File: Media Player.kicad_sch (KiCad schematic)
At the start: 33 parts, among them J1 PH2.0, J2 MEM2075-00-140-01-A, J3 USB_C_Receptacle_USB2.0_14P, SW1 SW_Push, SW2 SW_Push, SW3 SW_Push, SW4 SW_Push, SW5 SW_Push, SW6 SW_Push, U1 ESP32-S3-WROOM-1

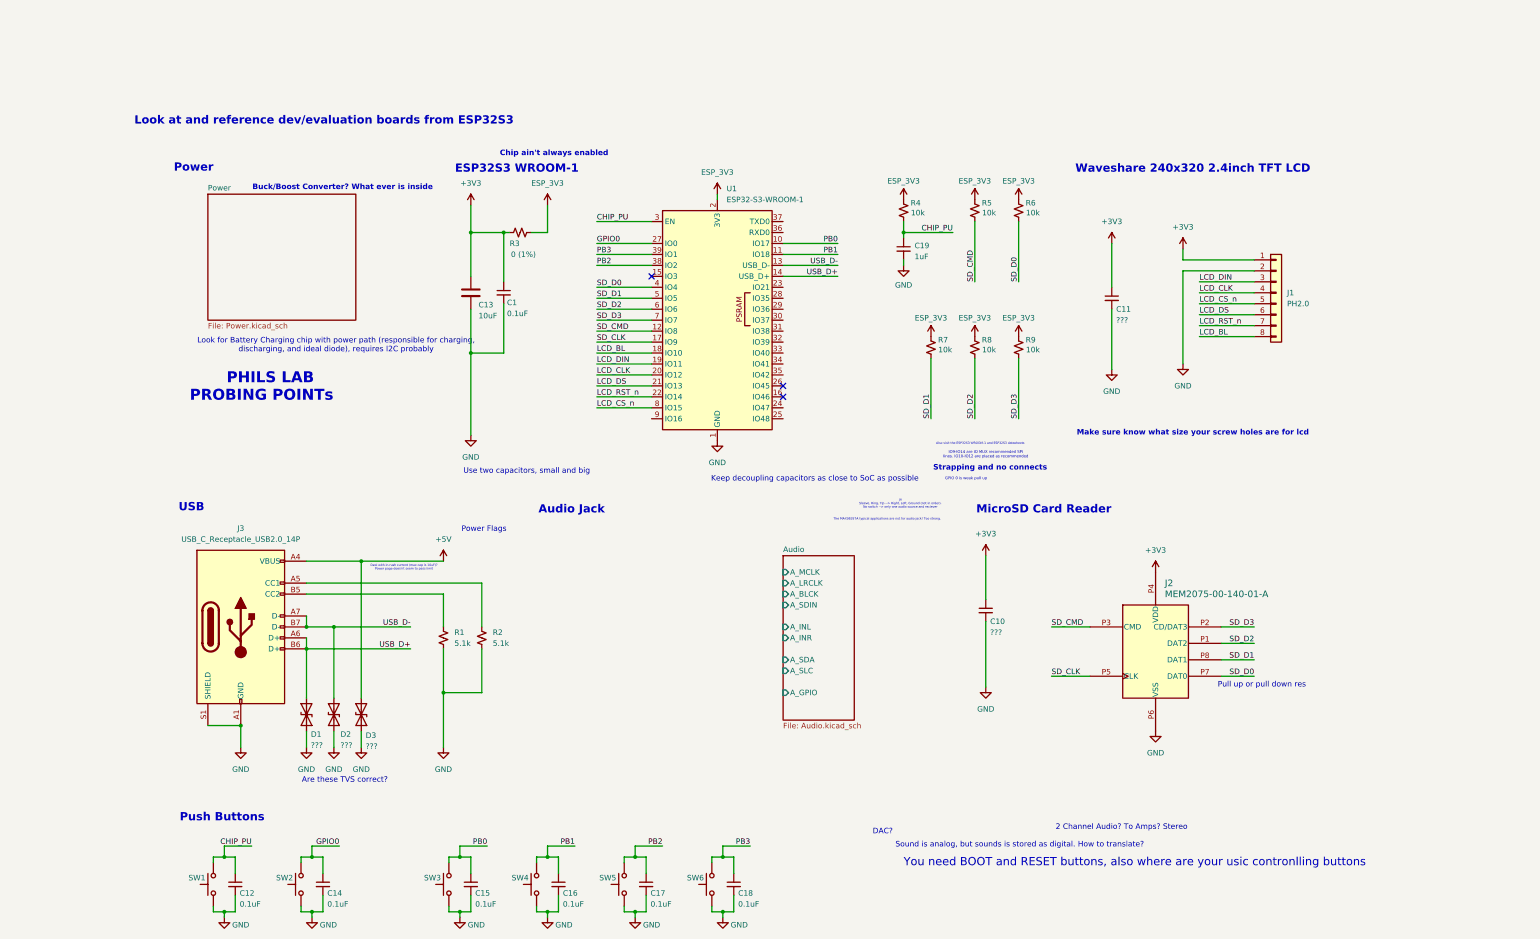
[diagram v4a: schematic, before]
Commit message: Draft 1 - Main components and wiring complete
Connections may be innacurate or violate electrical specs, or perhaps aren't set up "properly".
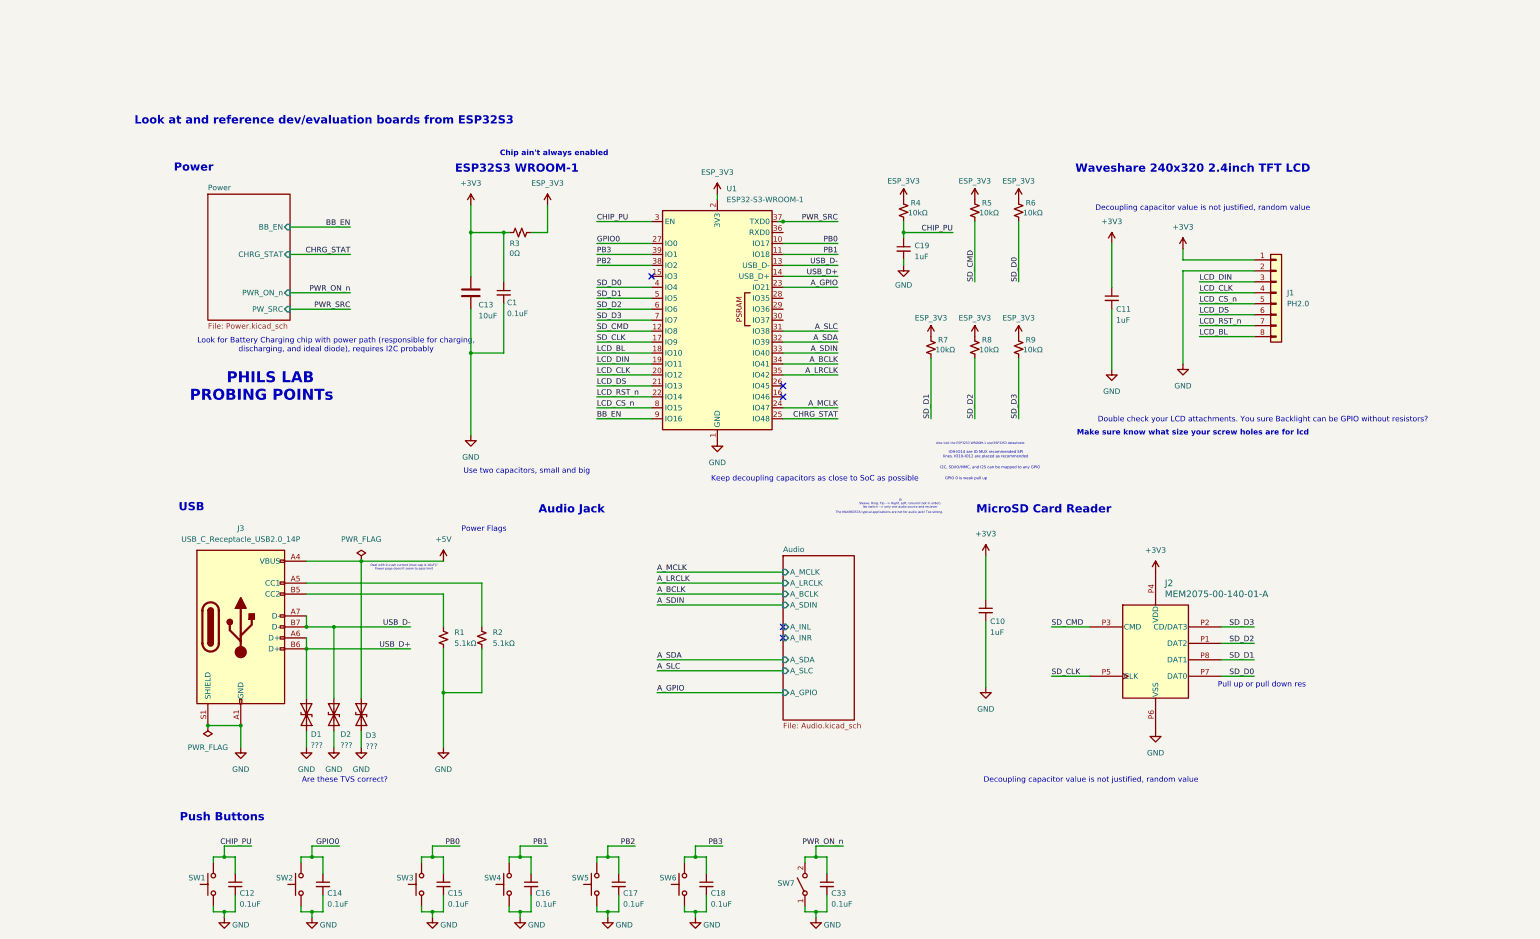
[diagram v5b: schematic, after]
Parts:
- added C33: 0.1uF, symbol Device:C_Small
- added SW7: SW_SPST, symbol Switch:SW_SPST
- C10, C11: value ??? -> 1uF
- R1, R2: value 5.1k -> 5.1kΩ
- R3: value 0 (1%) -> 0Ω
- R4, R5, R6, R7, R8, R9: value 10k -> 10kΩ
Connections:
- net GND: now also C33.2, SW7.1 (A)
- net A_GPIO: now reaches U1.23 (IO21)
- net A_MCLK: now reaches U1.24 (IO47)
- net CHRG_STAT: now reaches U1.25 (IO48)
- net A_SLC: now reaches U1.31 (IO38)
- net A_SDA: now reaches U1.32 (IO39)
- net A_SDIN: now reaches U1.33 (IO40)
- net A_BCLK: now reaches U1.34 (IO41)
- net A_LRCLK: now reaches U1.35 (IO42)
- net PWR_SRC: now reaches U1.37 (TXD0)
- net BB_EN: now reaches U1.9 (IO16)
- new net PWR_ON_n: C33.1, SW7.2 (B)
- no-connect marks 3 -> 5
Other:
- sheet Audio ports: added A_BCLK; removed A_BLCK
- sheet Power ports: added BB_EN, CHRG_STAT, PWR_ON_n, PW_SRC; removed none
- note added: "Decoupling capacitor value is not justified, random value"
- note added: "Double check your LCD attachments. You sure Backlight can be GPIO without resistors?"
- note added: "I2C, SD/IO/MMC, and I2S can be mapped to any GPIO"
- note removed: "2 Channel Audio? To Amps? Stereo"
- note removed: "Buck/Boost Converter? What ever is inside"
- note removed: "DAC?"
- note removed: "Sound is analog, but sounds is stored as digital. How to translate?"
- note removed: "Strapping and no connects"
- note removed: "You need BOOT and RESET buttons, also where are your usic contronlling buttons"
- moved on the sheet: C15, C16, C17, C18, SW3, SW4, SW5, SW6

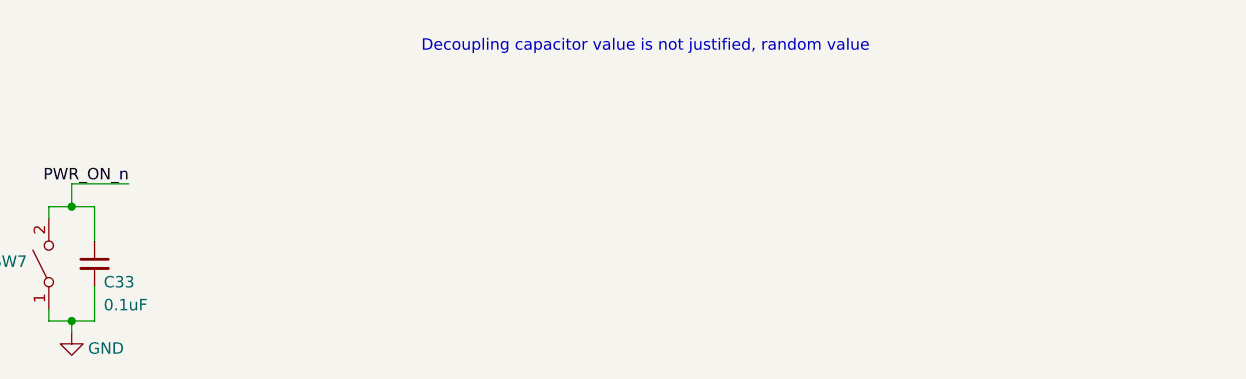
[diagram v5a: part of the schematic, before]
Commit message: Added missing datasheets.
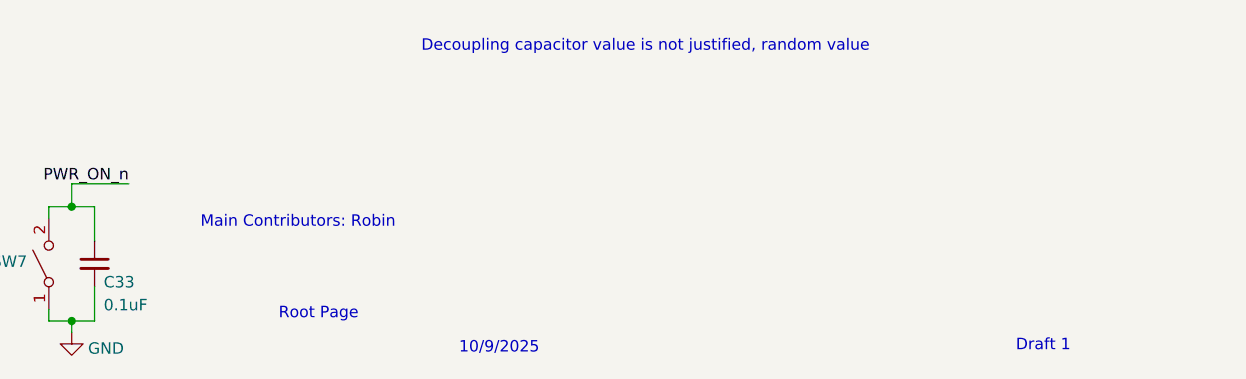
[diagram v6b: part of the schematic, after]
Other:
- note added: "10/9/2025"
- note added: "Draft 1"
- note added: "Main Contributors: Robin"
- note added: "Root Page"
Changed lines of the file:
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@@
 		)
 	)
+	(text "10/9/2025"
+		(exclude_from_sim no)
+		(at 212.598 193.548 0)
+		(effects
+			(font
+				(size 1.27 1.27)
+			)
+		)
+	)
+	(text "Root Page"
+		(exclude_from_sim no)
+		(at 192.532 189.738 0)
+		(effects
+			(font
+				(size 1.27 1.27)
+			)
+		)
+	)
 	(text "Pull up or pull down res\n"
 		(exclude_from_sim no)
@@
 		)
 	)
+	(text "Main Contributors: Robin"
+		(exclude_from_sim no)
+		(at 190.246 179.578 0)
+		(effects
+			(font
+				(size 1.27 1.27)
+			)
+		)
+	)
 	(text "PHILS LAB"
 		(exclude_from_sim no)
@@
 		)
 	)
+	(text "Draft 1"
+		(exclude_from_sim no)
+		(at 273.05 193.294 0)
+		(effects
+			(font
+				(size 1.27 1.27)
+			)
+		)
+	)
 	(text "USB\n"
 		(exclude_from_sim no)
@@
 			)
 		)
-		(property "Datasheet" "MEM2075-00-140-01-A"
+		(property "Datasheet" "https://gct.co/connector/mem2075"
 			(at 261.62 113.538 0)
 			(effects
@@
 			)
 		)
-		(property "Datasheet" "~"
+		(property "Datasheet" "https://www.waveshare.com/wiki/2.4inch_LCD_Module"
 			(at 271.78 46.99 0)
 			(effects

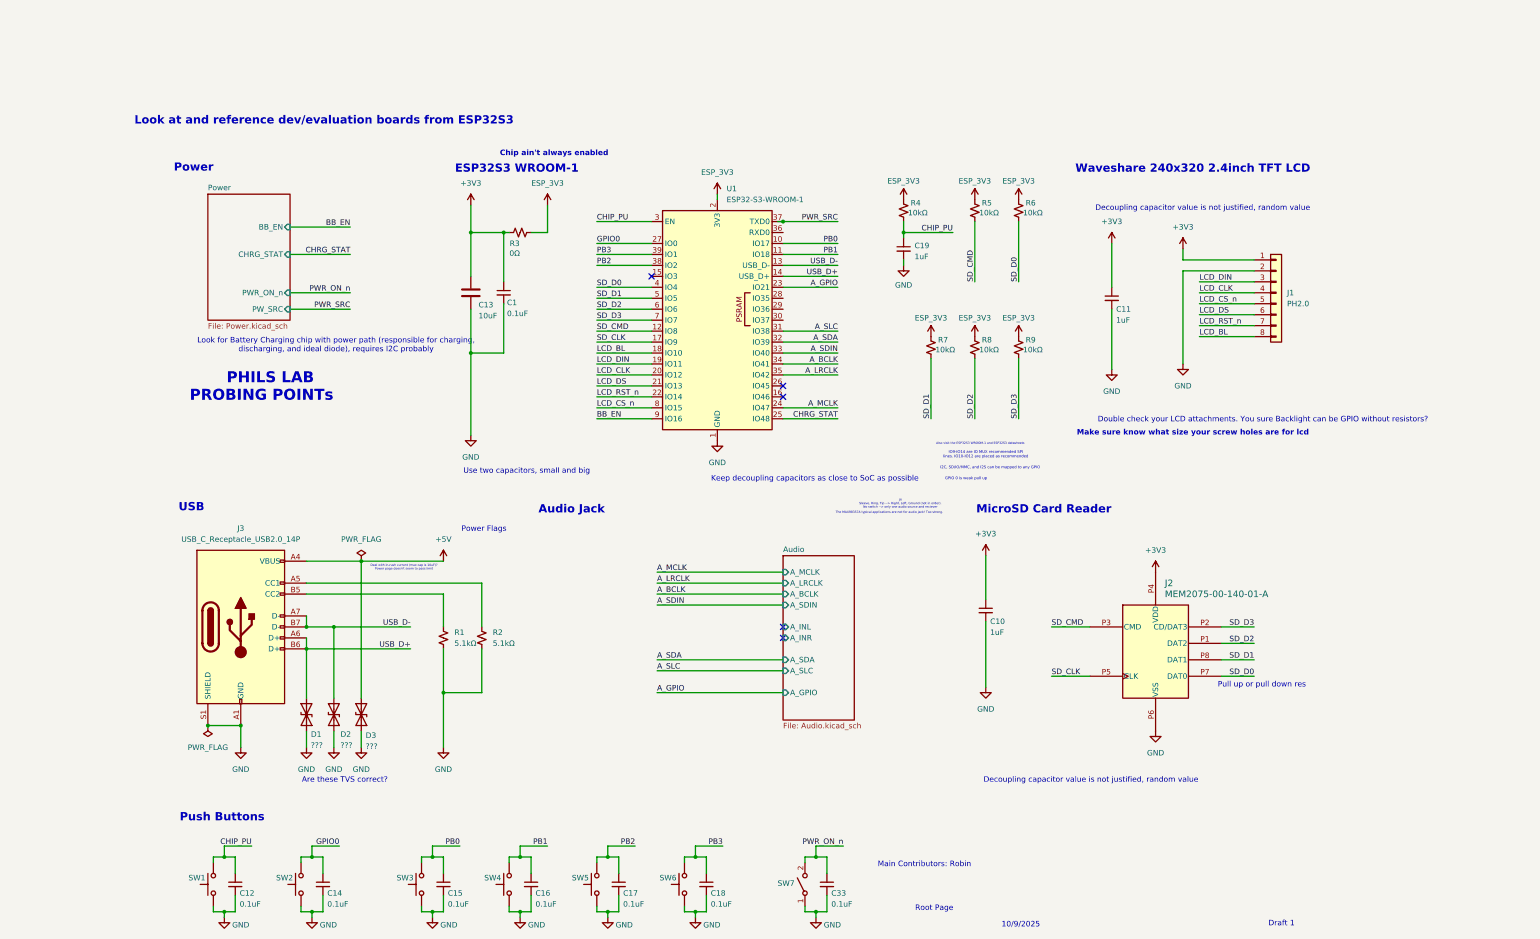
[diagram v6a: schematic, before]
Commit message: Added PMOS to battery + power flags
Still missing values for a lot of components
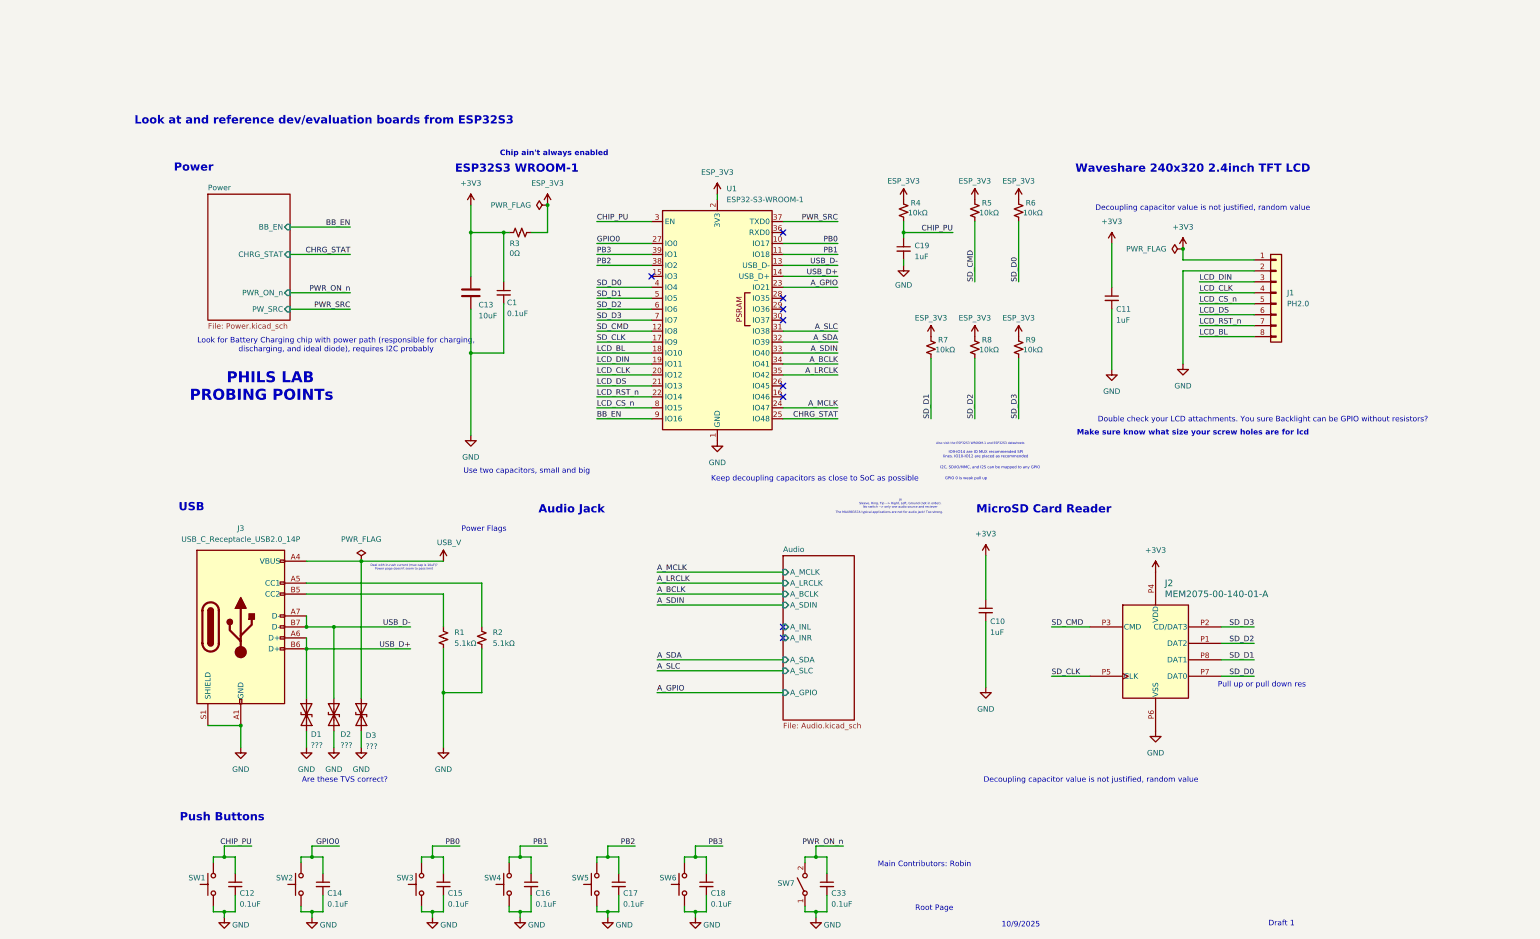
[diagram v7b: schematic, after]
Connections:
- net +5V renamed USB_V
- no-connect marks 5 -> 9
